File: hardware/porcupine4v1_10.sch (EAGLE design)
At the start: 28 parts, among them U1 USD-SOCKETNEW, X1 PROGCON

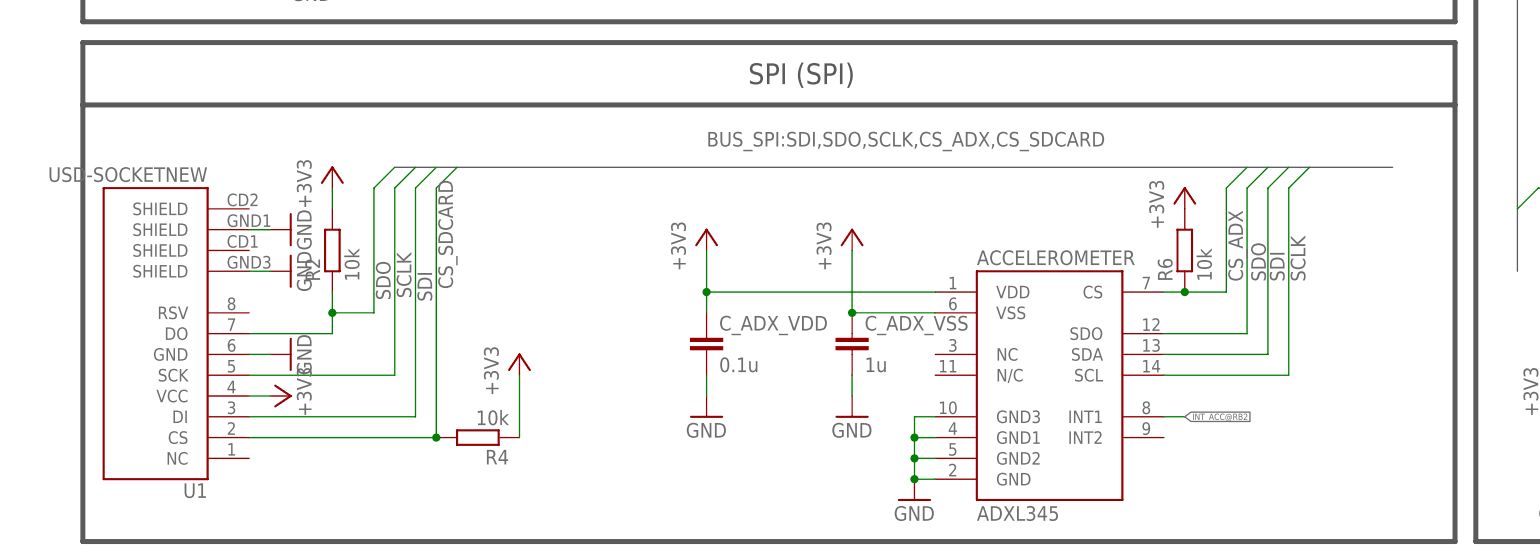
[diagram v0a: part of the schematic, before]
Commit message: v4.1.10 wiring optimized
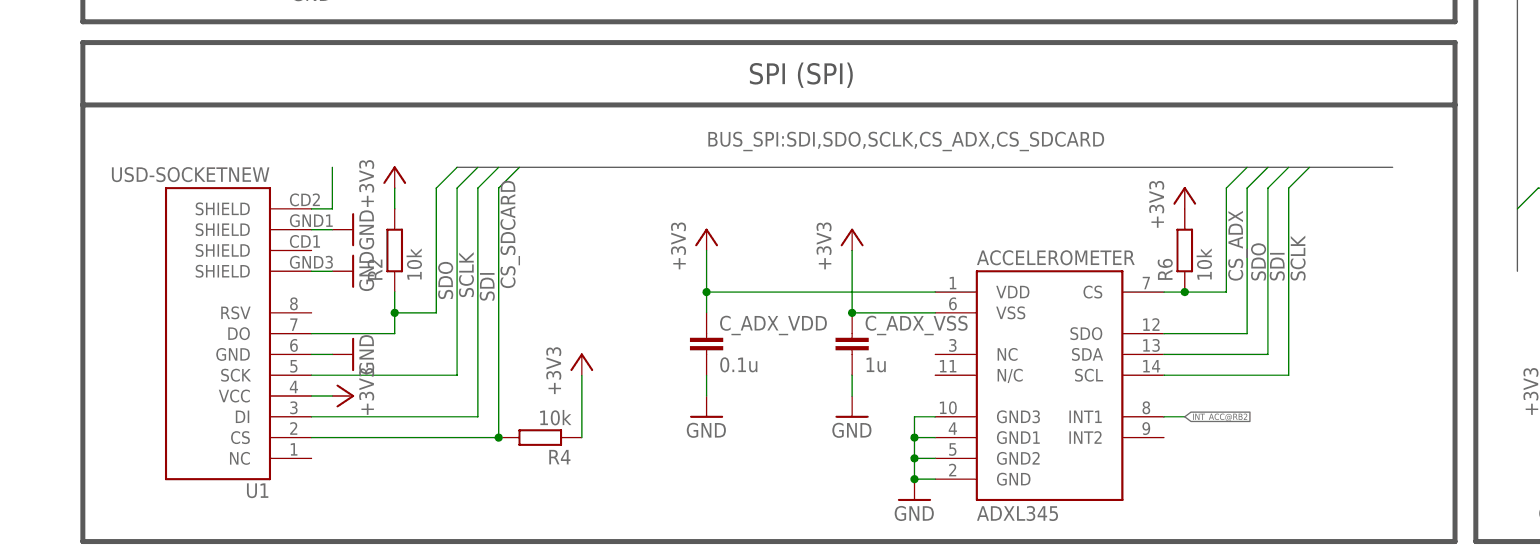
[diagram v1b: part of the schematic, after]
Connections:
- new net N$4: U1.SHIELD@4
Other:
- moved on the sheet: R2, R4, U1
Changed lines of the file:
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@@
 <?xml version="1.0" encoding="utf-8"?>
 <!DOCTYPE eagle SYSTEM "eagle.dtd">
-<eagle version="6.5.0">
+<eagle version="6.6.0">
 <drawing>
 <settings>
@@
 <attribute name="VALUE" x="264.16" y="86.36" size="1.778" layer="96" rot="R90"/>
 </instance>
-<instance part="R2" gate="G$1" x="33.02" y="38.1" rot="R90"/>
-<instance part="R4" gate="G$1" x="50.8" y="15.24" rot="R180"/>
-<instance part="+3V8" gate="G$1" x="33.02" y="48.26"/>
-<instance part="+3V10" gate="G$1" x="55.88" y="25.4"/>
+<instance part="R2" gate="G$1" x="40.64" y="38.1" rot="R90"/>
+<instance part="R4" gate="G$1" x="58.42" y="15.24" rot="R180"/>
+<instance part="+3V8" gate="G$1" x="40.64" y="48.26"/>
+<instance part="+3V10" gate="G$1" x="63.5" y="25.4"/>
 <instance part="C_UC_VDDCORE" gate="G$1" x="248.92" y="38.1"/>
 <instance part="X1" gate="-1" x="38.1" y="142.24" smashed="yes">
@@
 <attribute name="OC_FARNELL" x="127" y="93.98" size="1.778" layer="96" display="off"/>
 </instance>
-<instance part="U1" gate="G$1" x="15.24" y="25.4" rot="R180"/>
-<instance part="GND2" gate="1" x="27.94" y="25.4" rot="R90"/>
-<instance part="+3V12" gate="G$1" x="27.94" y="20.32" smashed="yes" rot="R270">
-<attribute name="VALUE" x="30.48" y="17.78" size="1.778" layer="96" rot="R90"/>
-</instance>
-<instance part="GND10" gate="1" x="27.94" y="40.64" rot="R90"/>
-<instance part="GND12" gate="1" x="27.94" y="35.56" rot="R90"/>
+<instance part="U1" gate="G$1" x="22.86" y="25.4" rot="R180"/>
+<instance part="GND2" gate="1" x="35.56" y="25.4" rot="R90"/>
+<instance part="+3V12" gate="G$1" x="35.56" y="20.32" smashed="yes" rot="R270">
+<attribute name="VALUE" x="38.1" y="17.78" size="1.778" layer="96" rot="R90"/>
+</instance>
+<instance part="GND10" gate="1" x="35.56" y="40.64" rot="R90"/>
+<instance part="GND12" gate="1" x="35.56" y="35.56" rot="R90"/>
 </instances>
 <busses>
@@
 </segment>
 <segment>
-<wire x1="40.64" y1="48.26" x2="162.56" y2="48.26" width="0.762" layer="92"/>
+<wire x1="48.26" y1="48.26" x2="162.56" y2="48.26" width="0.762" layer="92"/>
 <label x="78.74" y="50.8" size="1.778" layer="95"/>
 </segment>
@@
 <pinref part="U1" gate="G$1" pin="GND"/>
 <pinref part="GND2" gate="1" pin="GND"/>
-<wire x1="25.4" y1="25.4" x2="22.86" y2="25.4" width="0.1524" layer="91"/>
+<wire x1="33.02" y1="25.4" x2="30.48" y2="25.4" width="0.1524" layer="91"/>
 </segment>
 <segment>
 <pinref part="U1" gate="G$1" pin="SHIELD@3"/>
 <pinref part="GND10" gate="1" pin="GND"/>
-<wire x1="25.4" y1="40.64" x2="22.86" y2="40.64" width="0.1524" layer="91"/>
+<wire x1="33.02" y1="40.64" x2="30.48" y2="40.64" width="0.1524" layer="91"/>
 </segment>
 <segment>
 <pinref part="U1" gate="G$1" pin="SHIELD@1"/>
 <pinref part="GND12" gate="1" pin="GND"/>
-<wire x1="25.4" y1="35.56" x2="22.86" y2="35.56" width="0.1524" layer="91"/>
+<wire x1="33.02" y1="35.56" x2="30.48" y2="35.56" width="0.1524" layer="91"/>
 </segment>
 </net>
@@
 </segment>
 <segment>
-<wire x1="33.02" y1="45.72" x2="33.02" y2="43.18" width="0.1524" layer="91"/>
+<wire x1="40.64" y1="45.72" x2="40.64" y2="43.18" width="0.1524" layer="91"/>
 <pinref part="R2" gate="G$1" pin="2"/>
 <pinref part="+3V8" gate="G$1" pin="+3V3"/>
 </segment>
 <segment>
-<wire x1="55.88" y1="15.24" x2="55.88" y2="22.86" width="0.1524" layer="91"/>
+<wire x1="63.5" y1="15.24" x2="63.5" y2="22.86" width="0.1524" layer="91"/>
 <pinref part="R4" gate="G$1" pin="1"/>
 <pinref part="+3V10" gate="G$1" pin="+3V3"/>
@@
 <pinref part="U1" gate="G$1" pin="VCC"/>
 <pinref part="+3V12" gate="G$1" pin="+3V3"/>
-<wire x1="25.4" y1="20.32" x2="22.86" y2="20.32" width="0.1524" layer="91"/>
+<wire x1="33.02" y1="20.32" x2="30.48" y2="20.32" width="0.1524" layer="91"/>
 </segment>
 </net>
@@
 </segment>
 <segment>
-<wire x1="22.86" y1="17.78" x2="43.18" y2="17.78" width="0.1524" layer="91"/>
-<wire x1="43.18" y1="17.78" x2="43.18" y2="45.72" width="0.1524" layer="91"/>
-<wire x1="43.18" y1="45.72" x2="45.72" y2="48.26" width="0.1524" layer="91"/>
-<label x="43.434" y="35.56" size="1.778" layer="95" rot="R270"/>
+<wire x1="30.48" y1="17.78" x2="50.8" y2="17.78" width="0.1524" layer="91"/>
+<wire x1="50.8" y1="17.78" x2="50.8" y2="45.72" width="0.1524" layer="91"/>
+<wire x1="50.8" y1="45.72" x2="53.34" y2="48.26" width="0.1524" layer="91"/>
+<label x="51.054" y="35.56" size="1.778" layer="95" rot="R270"/>
 <pinref part="U1" gate="G$1" pin="DI"/>
 </segment>
@@
 </segment>
 <segment>
-<wire x1="38.1" y1="30.48" x2="38.1" y2="45.72" width="0.1524" layer="91"/>
-<wire x1="38.1" y1="45.72" x2="40.64" y2="48.26" width="0.1524" layer="91"/>
-<wire x1="33.02" y1="33.02" x2="33.02" y2="30.48" width="0.1524" layer="91"/>
-<wire x1="33.02" y1="30.48" x2="38.1" y2="30.48" width="0.1524" layer="91"/>
-<junction x="33.02" y="30.48"/>
-<label x="38.354" y="36.83" size="1.778" layer="95" rot="R270"/>
+<wire x1="45.72" y1="30.48" x2="45.72" y2="45.72" width="0.1524" layer="91"/>
+<wire x1="45.72" y1="45.72" x2="48.26" y2="48.26" width="0.1524" layer="91"/>
+<wire x1="40.64" y1="33.02" x2="40.64" y2="30.48" width="0.1524" layer="91"/>
+<wire x1="40.64" y1="30.48" x2="45.72" y2="30.48" width="0.1524" layer="91"/>
+<junction x="40.64" y="30.48"/>
+<label x="45.974" y="36.83" size="1.778" layer="95" rot="R270"/>
 <pinref part="R2" gate="G$1" pin="1"/>
-<wire x1="33.02" y1="30.48" x2="33.02" y2="27.94" width="0.1524" layer="91"/>
+<wire x1="40.64" y1="30.48" x2="40.64" y2="27.94" width="0.1524" layer="91"/>
 <pinref part="U1" gate="G$1" pin="DO"/>
-<wire x1="33.02" y1="27.94" x2="22.86" y2="27.94" width="0.1524" layer="91"/>
+<wire x1="40.64" y1="27.94" x2="30.48" y2="27.94" width="0.1524" layer="91"/>
 </segment>
 <segment>
@@
 </segment>
 <segment>
-<wire x1="40.64" y1="22.86" x2="40.64" y2="45.72" width="0.1524" layer="91"/>
-<wire x1="40.64" y1="45.72" x2="43.18" y2="48.26" width="0.1524" layer="91"/>
-<label x="40.894" y="37.846" size="1.778" layer="95" rot="R270"/>
+<wire x1="48.26" y1="22.86" x2="48.26" y2="45.72" width="0.1524" layer="91"/>
+<wire x1="48.26" y1="45.72" x2="50.8" y2="48.26" width="0.1524" layer="91"/>
+<label x="48.514" y="37.846" size="1.778" layer="95" rot="R270"/>
 <pinref part="U1" gate="G$1" pin="SCK"/>
-<wire x1="40.64" y1="22.86" x2="22.86" y2="22.86" width="0.1524" layer="91"/>
+<wire x1="48.26" y1="22.86" x2="30.48" y2="22.86" width="0.1524" layer="91"/>
 </segment>
 <segment>
@@
 <net name="CS_SDCARD" class="0">
 <segment>
-<wire x1="22.86" y1="15.24" x2="45.72" y2="15.24" width="0.1524" layer="91"/>
-<wire x1="45.72" y1="15.24" x2="45.72" y2="45.72" width="0.1524" layer="91"/>
-<wire x1="45.72" y1="45.72" x2="48.26" y2="48.26" width="0.1524" layer="91"/>
-<junction x="45.72" y="15.24"/>
-<label x="45.974" y="46.736" size="1.778" layer="95" rot="R270"/>
+<wire x1="30.48" y1="15.24" x2="53.34" y2="15.24" width="0.1524" layer="91"/>
+<wire x1="53.34" y1="15.24" x2="53.34" y2="45.72" width="0.1524" layer="91"/>
+<wire x1="53.34" y1="45.72" x2="55.88" y2="48.26" width="0.1524" layer="91"/>
+<junction x="53.34" y="15.24"/>
+<label x="53.594" y="46.736" size="1.778" layer="95" rot="R270"/>
 <pinref part="R4" gate="G$1" pin="2"/>
 <pinref part="U1" gate="G$1" pin="CS"/>
@@
 </segment>
 </net>
+<net name="N$4" class="0">
+<segment>
+<pinref part="U1" gate="G$1" pin="SHIELD@4"/>
+<wire x1="30.48" y1="43.18" x2="33.02" y2="43.18" width="0.1524" layer="91"/>
+<wire x1="33.02" y1="43.18" x2="33.02" y2="48.26" width="0.1524" layer="91"/>
+</segment>
+</net>
